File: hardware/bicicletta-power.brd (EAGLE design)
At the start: 160 x 100 mm, 24 parts, among them IC1 LM5017, IC2 LM1117-3.3

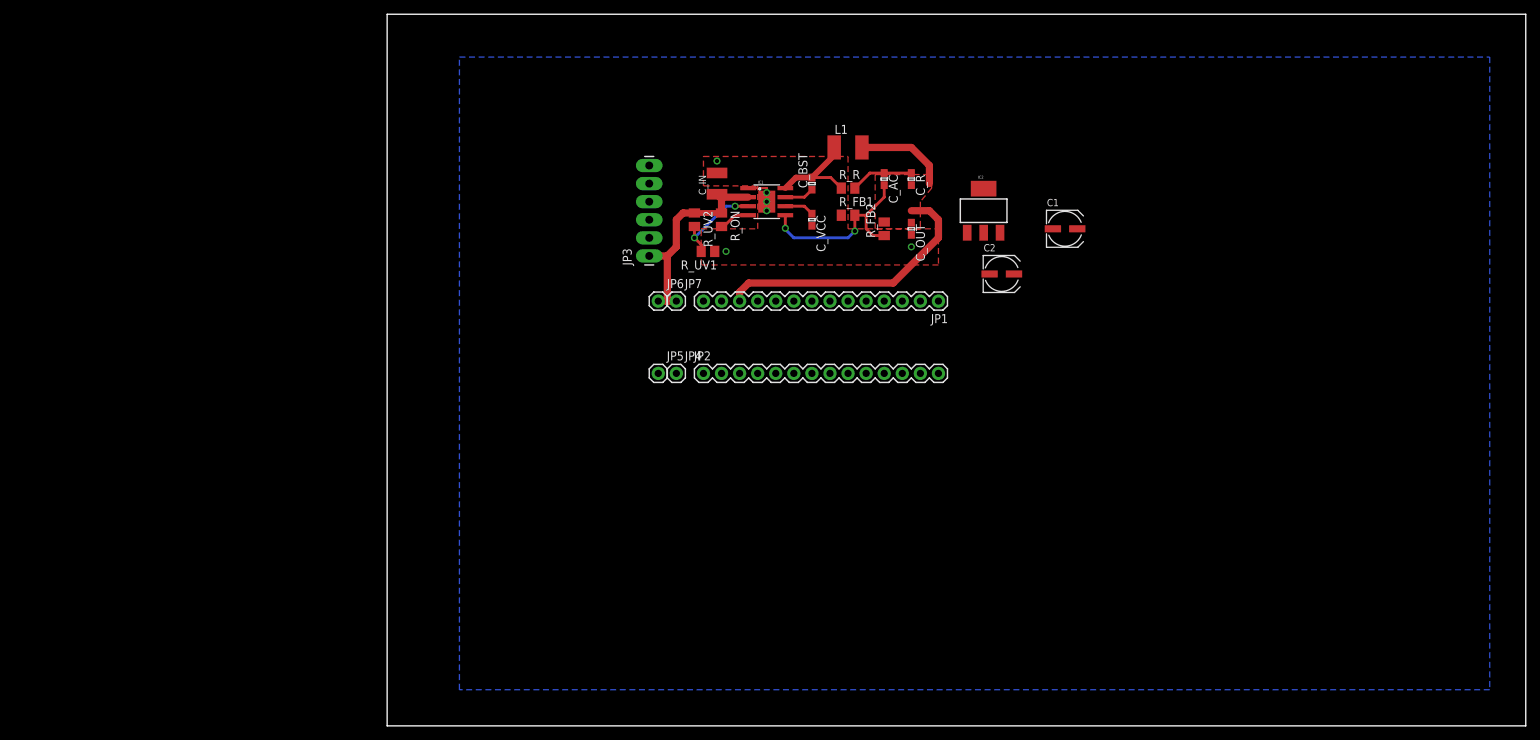
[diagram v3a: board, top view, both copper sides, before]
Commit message: Updated to include actual component for the BLEND MICRO
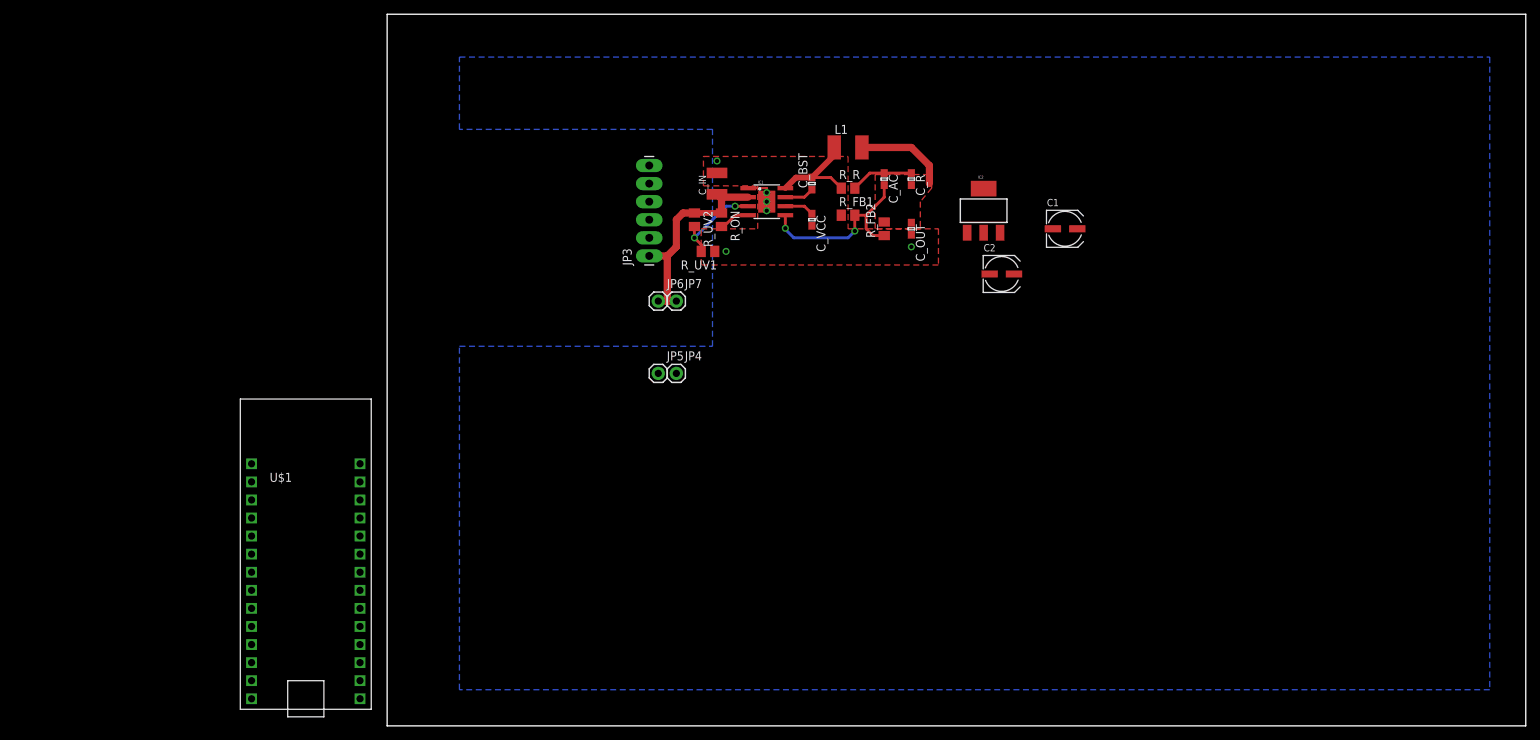
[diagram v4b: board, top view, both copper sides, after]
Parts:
- removed JP1, JP2: M14, SparkFun-Connectors:1X14
- added U$1: BLEND_MICRO, Railstars:BLEND_MICRO
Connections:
- net !RST: now also U$1.P$7; no longer JP1.7
- net 5V: now also U$1.P$12; no longer JP1.12
- net A0: now also U$1.P$23; no longer JP2.9
- net A1: now also U$1.P$22; no longer JP2.8
- net A2: now also U$1.P$21; no longer JP2.7
- net A3: now also U$1.P$20; no longer JP2.6
- net A4: now also U$1.P$19; no longer JP2.5
- net A5: now also U$1.P$18; no longer JP2.4
- net AREF: now also U$1.P$17; no longer JP2.3
- net CLK: now also U$1.P$10; no longer JP1.10
- net D0/RX: now also U$1.P$6; no longer JP1.6
- net D1/TX: now also U$1.P$5; no longer JP1.5
- net D12/A11: now also U$1.P$25; no longer JP2.11
- net D2/SDA: now also U$1.P$4; no longer JP1.4
- net D8/A8: now also U$1.P$1; no longer JP1.1
- net GND: now also U$1.P$13, U$1.P$14, U$1.P$15; no longer JP1.13, JP1.14, JP2.1
- net MISO: now also U$1.P$8; no longer JP1.8
- net MOSI: now also U$1.P$9; no longer JP1.9
- net SHUNT-: now also JP5.1
- net SS: now also U$1.P$11; no longer JP1.11
- net ~D10/A10: now also U$1.P$27; no longer JP2.13
- net ~D11: now also U$1.P$26; no longer JP2.12
- net ~D13/LED: now also U$1.P$24; no longer JP2.10
- net ~D3/SCL: now also U$1.P$3; no longer JP1.3
- net ~D5: now also U$1.P$2; no longer JP1.2
- net ~D9/A9: now also U$1.P$28; no longer JP2.14
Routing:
- net 5V: track 52.3 -> 13.1 mm
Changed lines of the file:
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@@
 </autorouter>
 <elements>
-<element name="JP1" library="SparkFun-Connectors" package="1X14" value="M14" x="77.47" y="59.69" rot="R180"/>
-<element name="JP2" library="SparkFun-Connectors" package="1X14" value="M14" x="44.45" y="49.53"/>
 <element name="IC1" library="Railstars" package="SOIC-8-POWERPAD" value="LM5017" x="53.34" y="73.66" rot="R270"/>
 <element name="R_ON" library="rcl" package="M0805" value="250K" x="46.99" y="71.12" rot="R270"/>
@@
 <element name="JP6" library="SparkFun-Connectors" package="1X01" value="M01PTH" x="38.1" y="59.69"/>
 <element name="JP7" library="SparkFun-Connectors" package="1X01" value="M01PTH" x="40.64" y="59.69"/>
+<element name="U$1" library="Railstars" package="BLEND_MICRO" value="BLEND_MICRO" x="-11.43" y="24.13"/>
 </elements>
 <signals>
-<signal name="D8/A8">
-<contactref element="JP1" pad="1"/>
-</signal>
-<signal name="~D5">
-<contactref element="JP1" pad="2"/>
-</signal>
-<signal name="~D3/SCL">
-<contactref element="JP1" pad="3"/>
-</signal>
-<signal name="D2/SDA">
-<contactref element="JP1" pad="4"/>
-</signal>
-<signal name="D1/TX">
-<contactref element="JP1" pad="5"/>
-</signal>
-<signal name="D0/RX">
-<contactref element="JP1" pad="6"/>
-</signal>
-<signal name="!RST">
-<contactref element="JP1" pad="7"/>
-</signal>
-<signal name="MISO">
-<contactref element="JP1" pad="8"/>
-</signal>
-<signal name="MOSI">
-<contactref element="JP1" pad="9"/>
-</signal>
-<signal name="CLK">
-<contactref element="JP1" pad="10"/>
-</signal>
-<signal name="SS">
-<contactref element="JP1" pad="11"/>
-</signal>
 <signal name="GND">
-<contactref element="JP1" pad="13"/>
-<contactref element="JP1" pad="14"/>
-<contactref element="JP2" pad="1"/>
 <contactref element="IC1" pad="1"/>
 <contactref element="IC1" pad="P$1"/>
@@
 <vertex x="154.94" y="5.08"/>
 <vertex x="10.16" y="5.08"/>
+<vertex x="10.16" y="53.34"/>
+<vertex x="45.72" y="53.34"/>
+<vertex x="45.72" y="83.82"/>
+<vertex x="10.16" y="83.82"/>
 </polygon>
 <polygon width="0.4064" layer="1" thermals="no">
@@
 <via x="46.355" y="79.375" extent="1-16" drill="0.6"/>
 <via x="47.625" y="66.675" extent="1-16" drill="0.6"/>
+<contactref element="U$1" pad="P$13"/>
+<contactref element="U$1" pad="P$14"/>
+<contactref element="U$1" pad="P$15"/>
 <wire x1="84.66" y1="63.5" x2="93.55" y2="69.85" width="0" layer="19" extent="1-1"/>
 <wire x1="81.5086" y1="69.2912" x2="84.66" y2="63.5" width="0" layer="19" extent="1-1"/>
 <wire x1="73.66" y1="69" x2="81.5086" y2="69.2912" width="0" layer="19" extent="1-1"/>
-</signal>
-<signal name="~D9/A9">
-<contactref element="JP2" pad="14"/>
-</signal>
-<signal name="~D10/A10">
-<contactref element="JP2" pad="13"/>
-</signal>
-<signal name="~D11">
-<contactref element="JP2" pad="12"/>
-</signal>
-<signal name="D12/A11">
-<contactref element="JP2" pad="11"/>
-</signal>
-<signal name="~D13/LED">
-<contactref element="JP2" pad="10"/>
-</signal>
-<signal name="A0">
-<contactref element="JP2" pad="9"/>
-</signal>
-<signal name="A1">
-<contactref element="JP2" pad="8"/>
-</signal>
-<signal name="A2">
-<contactref element="JP2" pad="7"/>
-</signal>
-<signal name="A3">
-<contactref element="JP2" pad="6"/>
-</signal>
-<signal name="A4">
-<contactref element="JP2" pad="5"/>
-</signal>
-<signal name="A5">
-<contactref element="JP2" pad="4"/>
-</signal>
-<signal name="AREF">
-<contactref element="JP2" pad="3"/>
+<wire x1="73.66" y1="67.31" x2="73.66" y2="69" width="0" layer="19" extent="1-1"/>
+<wire x1="63.82" y1="71.755" x2="73.66" y2="69" width="0" layer="19" extent="1-1"/>
+<wire x1="59.69" y1="70.27" x2="63.82" y2="71.755" width="0" layer="19" extent="1-1"/>
+<wire x1="53.34" y1="72.39" x2="59.69" y2="70.27" width="0" layer="19" extent="1-1"/>
+<wire x1="53.34" y1="73.66" x2="53.34" y2="72.39" width="0" layer="19" extent="1-1"/>
+<wire x1="53.34" y1="74.93" x2="53.34" y2="73.66" width="0" layer="19" extent="1-1"/>
+<wire x1="46.355" y1="77.7" x2="50.7238" y2="75.565" width="0" layer="19" extent="1-1"/>
+<wire x1="46.355" y1="79.375" x2="46.355" y2="77.7" width="0" layer="19" extent="1-1"/>
+<wire x1="47.625" y1="66.675" x2="53.34" y2="72.39" width="0" layer="19" extent="1-1"/>
+<wire x1="46.035" y1="66.675" x2="47.625" y2="66.675" width="0" layer="19" extent="1-1"/>
+<wire x1="36.83" y1="68.58" x2="46.035" y2="66.675" width="0" layer="19" extent="1-1"/>
+<wire x1="-3.81" y1="3.81" x2="36.83" y2="68.58" width="0" layer="19" extent="1-1"/>
+<wire x1="-19.05" y1="3.81" x2="-3.81" y2="3.81" width="0" layer="19" extent="1-1"/>
+<wire x1="-19.05" y1="6.35" x2="-19.05" y2="3.81" width="0" layer="19" extent="1-1"/>
 </signal>
 <signal name="V_BATT">
@@
 </signal>
 <signal name="5V">
-<contactref element="JP1" pad="12"/>
 <contactref element="IC2" pad="3"/>
 <contactref element="C1" pad="+"/>
@@
 <wire x1="73.66" y1="81.28" x2="76.2" y2="78.74" width="1.016" layer="1"/>
 <wire x1="76.2" y1="78.74" x2="76.2" y2="76.2" width="1.016" layer="1"/>
-<wire x1="49.53" y1="59.69" x2="49.53" y2="60.96" width="1.016" layer="1"/>
-<wire x1="49.53" y1="60.96" x2="50.8" y2="62.23" width="1.016" layer="1"/>
-<wire x1="50.8" y1="62.23" x2="71.12" y2="62.23" width="1.016" layer="1"/>
-<wire x1="71.12" y1="62.23" x2="77.47" y2="68.58" width="1.016" layer="1"/>
-<wire x1="77.47" y1="68.58" x2="77.47" y2="71.12" width="1.016" layer="1"/>
-<wire x1="77.47" y1="71.12" x2="76.2" y2="72.39" width="1.016" layer="1"/>
-<wire x1="76.2" y1="72.39" x2="73.66" y2="72.39" width="1.016" layer="1"/>
+<contactref element="U$1" pad="P$12"/>
 <wire x1="86.1314" y1="69.2912" x2="96.975" y2="69.85" width="0" layer="19" extent="1-1"/>
-<wire x1="77.47" y1="68.58" x2="86.1314" y2="69.2912" width="0" layer="19" extent="1-1"/>
+<wire x1="76.2" y1="76.2" x2="86.1314" y2="69.2912" width="0" layer="19" extent="1-1"/>
+<wire x1="73.66" y1="75.985" x2="76.2" y2="76.2" width="0" layer="19" extent="1-1"/>
+<wire x1="73.66" y1="70.7" x2="73.66" y2="75.985" width="0" layer="19" extent="1-1"/>
+<wire x1="69.85" y1="70.8" x2="73.66" y2="70.7" width="0" layer="19" extent="1-1"/>
+<wire x1="-19.05" y1="8.89" x2="69.85" y2="70.8" width="0" layer="19" extent="1-1"/>
 </signal>
 <signal name="N$1">
@@
 <signal name="SHUNT-">
 <contactref element="JP3" pad="3"/>
+<contactref element="JP5" pad="1"/>
+<wire x1="38.1" y1="49.53" x2="36.83" y2="71.12" width="0" layer="19" extent="1-1"/>
 </signal>
 <signal name="SHUNT+">
@@
 <contactref element="JP3" pad="6"/>
 </signal>
+<signal name="D8/A8">
+<contactref element="U$1" pad="P$1"/>
+</signal>
+<signal name="~D5">
+<contactref element="U$1" pad="P$2"/>
+</signal>
+<signal name="~D3/SCL">
+<contactref element="U$1" pad="P$3"/>
+</signal>
+<signal name="D2/SDA">
+<contactref element="U$1" pad="P$4"/>
+</signal>
+<signal name="D1/TX">
+<contactref element="U$1" pad="P$5"/>
+</signal>
+<signal name="D0/RX">
+<contactref element="U$1" pad="P$6"/>
+</signal>
+<signal name="!RST">
+<contactref element="U$1" pad="P$7"/>
+</signal>
+<signal name="MISO">
+<contactref element="U$1" pad="P$8"/>
+</signal>
+<signal name="MOSI">
+<contactref element="U$1" pad="P$9"/>
+</signal>
+<signal name="CLK">
+<contactref element="U$1" pad="P$10"/>
+</signal>
+<signal name="SS">
+<contactref element="U$1" pad="P$11"/>
+</signal>
+<signal name="~D9/A9">
+<contactref element="U$1" pad="P$28"/>
+</signal>
+<signal name="~D10/A10">
+<contactref element="U$1" pad="P$27"/>
+</signal>
+<signal name="~D11">
+<contactref element="U$1" pad="P$26"/>
+</signal>
+<signal name="D12/A11">
+<contactref element="U$1" pad="P$25"/>
+</signal>
+<signal name="~D13/LED">
+<contactref element="U$1" pad="P$24"/>
+</signal>
+<signal name="A0">
+<contactref element="U$1" pad="P$23"/>
+</signal>
+<signal name="A1">
+<contactref element="U$1" pad="P$22"/>
+</signal>
+<signal name="A2">
+<contactref element="U$1" pad="P$21"/>
+</signal>
+<signal name="A3">
+<contactref element="U$1" pad="P$20"/>
+</signal>
+<signal name="A4">
+<contactref element="U$1" pad="P$19"/>
+</signal>
+<signal name="A5">
+<contactref element="U$1" pad="P$18"/>
+</signal>
+<signal name="AREF">
+<contactref element="U$1" pad="P$17"/>
+</signal>
 </signals>

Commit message: Wider voltage range on the op-amp level shifter, refinements on the PCB layout
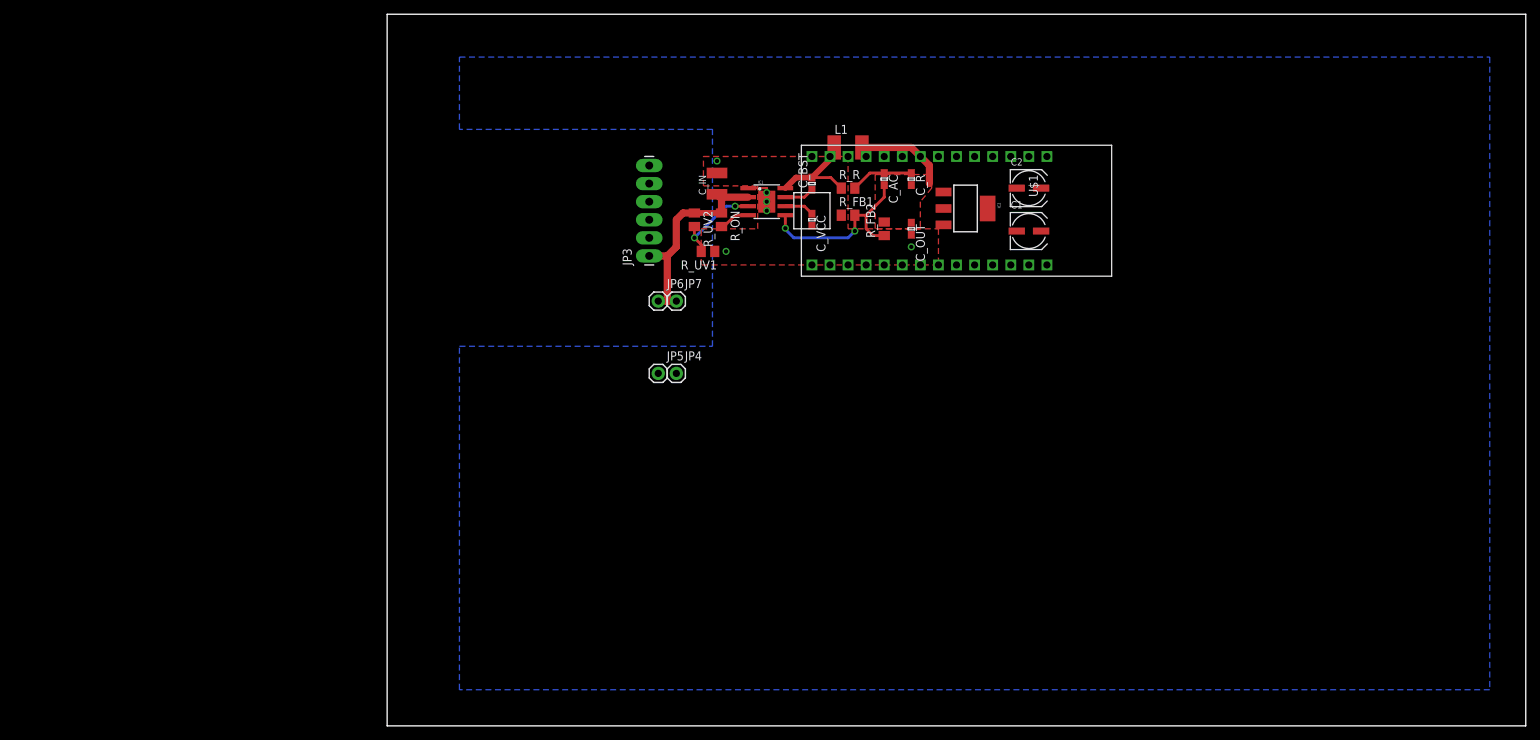
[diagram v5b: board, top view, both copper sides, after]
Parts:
- moved U$1 103.4 mm to (80.0, 72.4), turned to 270 degrees
- moved C2 12.7 mm to (90.2, 75.6)
- moved C1 5.09 mm to (90.2, 69.5)
- moved IC2 2.56 mm to (81.3, 72.7), turned to 270 degrees
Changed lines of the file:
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@@
 <element name="L1" library="rcl" package="L1812" value="100uH" x="64.77" y="81.28"/>
 <element name="R_R" library="rcl" package="M0805" value="2M" x="64.77" y="75.565"/>
-<element name="IC2" library="SparkFun-PowerIC" package="SOT223" value="LM1117-3.3" x="83.82" y="72.39"/>
-<element name="C1" library="rcl" package="UD-5X5,8_NICHICON" value="14uF" x="95.25" y="69.85"/>
-<element name="C2" library="rcl" package="UD-5X5,8_NICHICON" value="14uF" x="86.36" y="63.5"/>
+<element name="IC2" library="SparkFun-PowerIC" package="SOT223" value="LM1117-3.3" x="81.28" y="72.7075" rot="R270"/>
+<element name="C1" library="rcl" package="UD-5X5,8_NICHICON" value="14uF" x="90.17" y="69.5325"/>
+<element name="C2" library="rcl" package="UD-5X5,8_NICHICON" value="14uF" x="90.17" y="75.565"/>
 <element name="C_R" library="rcl" package="C0603" value="3300pF" x="73.66" y="76.835" rot="R270"/>
 <element name="C_AC" library="rcl" package="C0603" value="100nF" x="69.85" y="76.835" rot="R270"/>
@@
 <element name="JP6" library="SparkFun-Connectors" package="1X01" value="M01PTH" x="38.1" y="59.69"/>
 <element name="JP7" library="SparkFun-Connectors" package="1X01" value="M01PTH" x="40.64" y="59.69"/>
-<element name="U$1" library="Railstars" package="BLEND_MICRO" value="BLEND_MICRO" x="-11.43" y="24.13"/>
+<element name="U$1" library="Railstars" package="BLEND_MICRO" value="BLEND_MICRO" x="80.01" y="72.39" rot="R270"/>
 </elements>
 <signals>
@@
 <contactref element="U$1" pad="P$14"/>
 <contactref element="U$1" pad="P$15"/>
-<wire x1="84.66" y1="63.5" x2="93.55" y2="69.85" width="0" layer="19" extent="1-1"/>
-<wire x1="81.5086" y1="69.2912" x2="84.66" y2="63.5" width="0" layer="19" extent="1-1"/>
-<wire x1="73.66" y1="69" x2="81.5086" y2="69.2912" width="0" layer="19" extent="1-1"/>
+<wire x1="88.47" y1="75.565" x2="88.47" y2="69.5325" width="0" layer="19" extent="1-1"/>
+<wire x1="78.1812" y1="75.0189" x2="88.47" y2="75.565" width="0" layer="19" extent="1-1"/>
+<wire x1="73.66" y1="69" x2="78.1812" y2="75.0189" width="0" layer="19" extent="1-1"/>
 <wire x1="73.66" y1="67.31" x2="73.66" y2="69" width="0" layer="19" extent="1-1"/>
 <wire x1="63.82" y1="71.755" x2="73.66" y2="69" width="0" layer="19" extent="1-1"/>
@@
 <wire x1="46.035" y1="66.675" x2="47.625" y2="66.675" width="0" layer="19" extent="1-1"/>
 <wire x1="36.83" y1="68.58" x2="46.035" y2="66.675" width="0" layer="19" extent="1-1"/>
-<wire x1="-3.81" y1="3.81" x2="36.83" y2="68.58" width="0" layer="19" extent="1-1"/>
-<wire x1="-19.05" y1="3.81" x2="-3.81" y2="3.81" width="0" layer="19" extent="1-1"/>
-<wire x1="-19.05" y1="6.35" x2="-19.05" y2="3.81" width="0" layer="19" extent="1-1"/>
+<wire x1="59.69" y1="64.77" x2="36.83" y2="68.58" width="0" layer="19" extent="1-1"/>
+<wire x1="59.69" y1="80.01" x2="59.69" y2="64.77" width="0" layer="19" extent="1-1"/>
+<wire x1="62.23" y1="80.01" x2="59.69" y2="80.01" width="0" layer="19" extent="1-1"/>
 </signal>
 <signal name="V_BATT">
@@
 <wire x1="76.2" y1="78.74" x2="76.2" y2="76.2" width="1.016" layer="1"/>
 <contactref element="U$1" pad="P$12"/>
-<wire x1="86.1314" y1="69.2912" x2="96.975" y2="69.85" width="0" layer="19" extent="1-1"/>
-<wire x1="76.2" y1="76.2" x2="86.1314" y2="69.2912" width="0" layer="19" extent="1-1"/>
+<wire x1="78.1812" y1="70.3961" x2="91.895" y2="69.5325" width="0" layer="19" extent="1-1"/>
+<wire x1="76.2" y1="76.2" x2="78.1812" y2="70.3961" width="0" layer="19" extent="1-1"/>
 <wire x1="73.66" y1="75.985" x2="76.2" y2="76.2" width="0" layer="19" extent="1-1"/>
 <wire x1="73.66" y1="70.7" x2="73.66" y2="75.985" width="0" layer="19" extent="1-1"/>
 <wire x1="69.85" y1="70.8" x2="73.66" y2="70.7" width="0" layer="19" extent="1-1"/>
-<wire x1="-19.05" y1="8.89" x2="69.85" y2="70.8" width="0" layer="19" extent="1-1"/>
+<wire x1="64.77" y1="80.01" x2="69.85" y2="70.8" width="0" layer="19" extent="1-1"/>
 </signal>
 <signal name="N$1">
@@
 <contactref element="IC2" pad="2"/>
 <contactref element="C2" pad="+"/>
-<wire x1="83.82" y1="69.2912" x2="83.82" y2="75.489" width="0" layer="19" extent="1-1"/>
-<wire x1="88.085" y1="63.5" x2="83.82" y2="69.2912" width="0" layer="19" extent="1-1"/>
+<wire x1="78.1812" y1="72.7075" x2="84.379" y2="72.7075" width="0" layer="19" extent="1-1"/>
+<wire x1="91.895" y1="75.565" x2="78.1812" y2="72.7075" width="0" layer="19" extent="1-1"/>
 </signal>
 <signal name="N$4">
